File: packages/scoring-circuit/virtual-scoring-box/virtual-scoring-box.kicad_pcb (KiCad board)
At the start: 4 copper layers, 120 x 85 mm, 146 parts, among them J1 GCT USB4105-GF-A, J2 STM SWD 3.3V, J3 LEFT WEAPON A B C, J4 RIGHT WEAPON A B C, J5 PISTE - NOT protective earth, J6 ESP 3.3V UART recovery, J7 PRIMARY SWD PADS, SW1 STM RESET, SW2 ESP RESET, SW3 ESP BOOT, T1 750315371, U1 STM32G474RET6, U13 TSOP38438, U18 CP2102N-A02-GQFN20R, U19 ISO7021DR, U2 ESP32-S3-WROOM-1-N8R8, U20 TPS70933DBVR, U21 SN6505BDBVR, U22 TPS62162DSGR, U23 STUSB4500QTR, U24 STM32C011F6P6, U25 TPS259470ARPWR, U26 SN74LVC1G3208DBVR, U27 SN74LVC1T45DBVR, U3 TPD2E2U06DCKR, U8 74LVC125APW, U9 74LVC125APW, Y1 ABM3B-8.000MHZ-B2-T

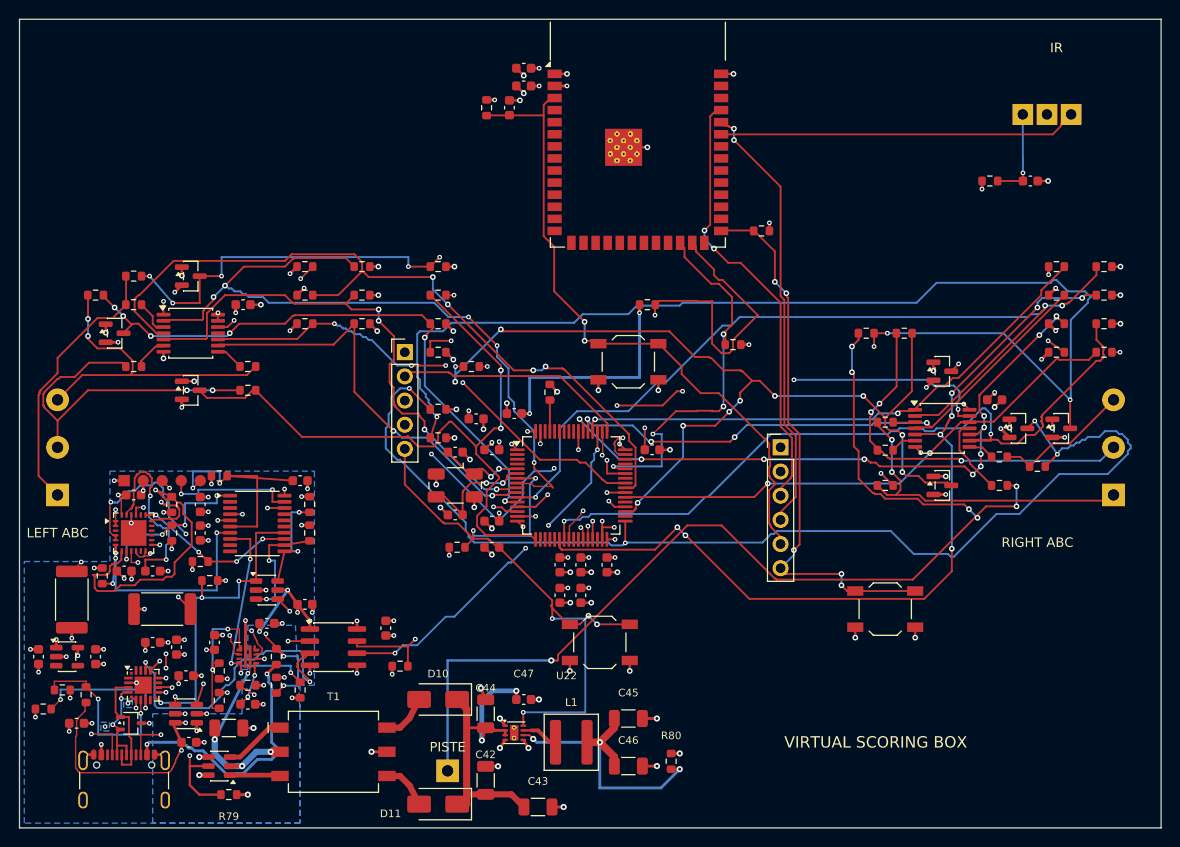
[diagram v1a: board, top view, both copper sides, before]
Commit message: fix(scoring-circuit): refine virtual-box layout and refresh assembly draft
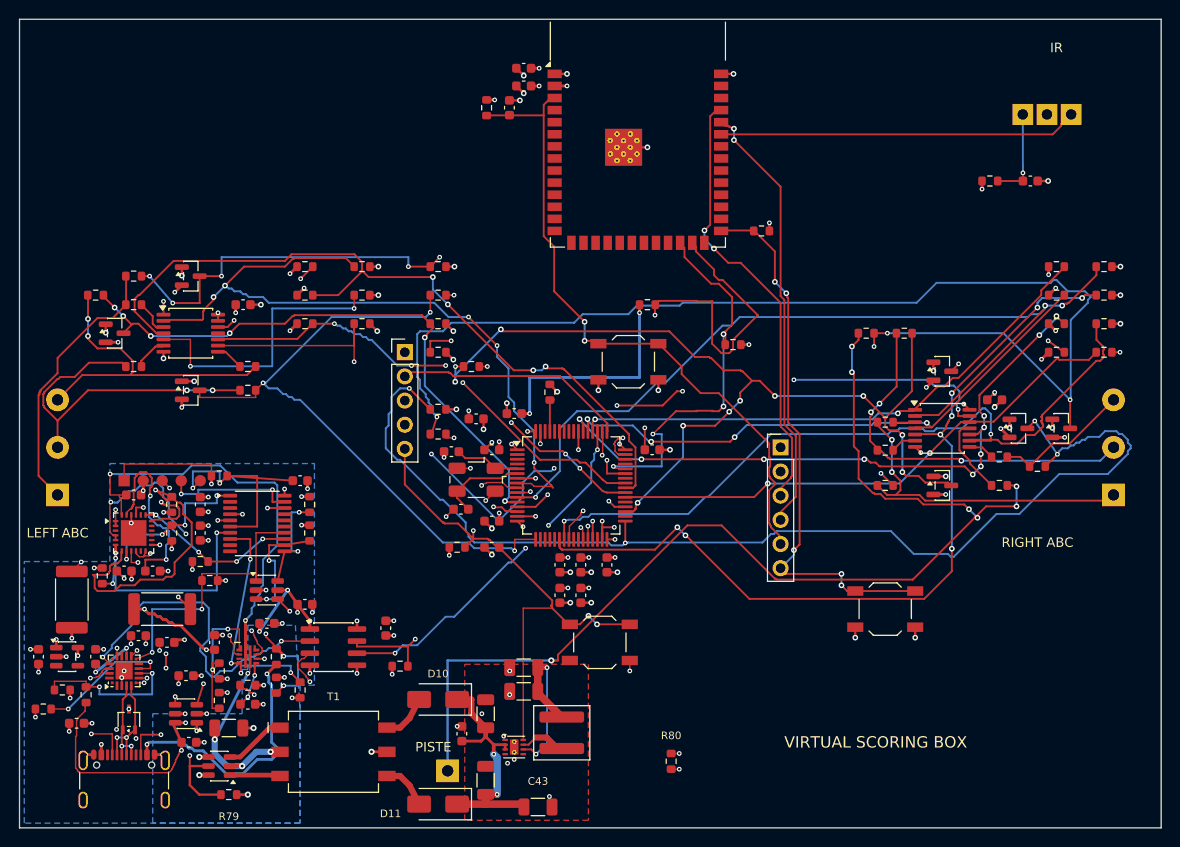
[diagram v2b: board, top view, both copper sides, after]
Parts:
- moved C46 15.1 mm to (103.0, 118.2), turned to 180 degrees
- moved C45 11.4 mm to (103.0, 120.7), turned to 180 degrees
- moved C47 7.43 mm to (96.5, 125.1), turned to 90 degrees
- moved C36 4.18 mm to (62.5, 114.8), turned to 0 degrees
- moved U18 2.50 mm to (61.0, 118.5), turned to 90 degrees
- moved Y1 2.28 mm to (98.0, 98.4)
- moved C35 1.50 mm to (65.5, 115.5)
- moved U22 1.50 mm to (102.0, 126.5)
- moved L1 1.41 mm to (107.0, 125.0), turned to 90 degrees
- moved C18 0.85 mm to (96.4, 101.5)
- moved U3 0.45 mm to (61.5, 123.6), turned to 90 degrees
- moved C17 0.40 mm to (95.4, 95.5), turned to 180 degrees
- moved R71 0.40 mm to (94.0, 93.6)
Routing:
- net USB_VBUS: track 74.3 -> 115.2 mm
- net LEFT_B_DRIVE: track 56.5 -> 77.6 mm, vias 4 -> 3
- net HOST_UART_RX: track 19.3 -> 35.8 mm
- net LEFT_A_OE_N: track 73.8 -> 89.8 mm, vias 3 -> 5
- net CORE_3V3: track 100.2 -> 88.5 mm
- net GND: track 87.0 -> 76.0 mm, vias 74 -> 72
- net HOST_UART_TX: track 32.9 -> 42.1 mm
- net USB_HOST_3V3: track 37.7 -> 46.0 mm
- net ISO_UNREG: track 34.1 -> 25.9 mm
- net USB_AWAKE: track 35.3 -> 29.9 mm, vias 3 -> 2
- net STM_RESET_N: track 74.2 -> 69.6 mm, vias 6 -> 4
- net LEFT_B_SENSE: track 72.6 -> 68.1 mm, vias 2 -> 3
- net LEFT_C_DRIVE: track 44.2 -> 48.2 mm
- net HSE_OUT: track 12.8 -> 9.48 mm, vias 2 -> 0
- net USB_HOST_DP: track 12.7 -> 9.40 mm, vias 0 -> 2
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- added copper zone on F.Cu, net GND
- added copper zone on In2.Cu, net USB_GND
- removed copper zone on B.Cu, net USB_GND

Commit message: refactor(scoring-circuit): organize virtual-box placement and routing
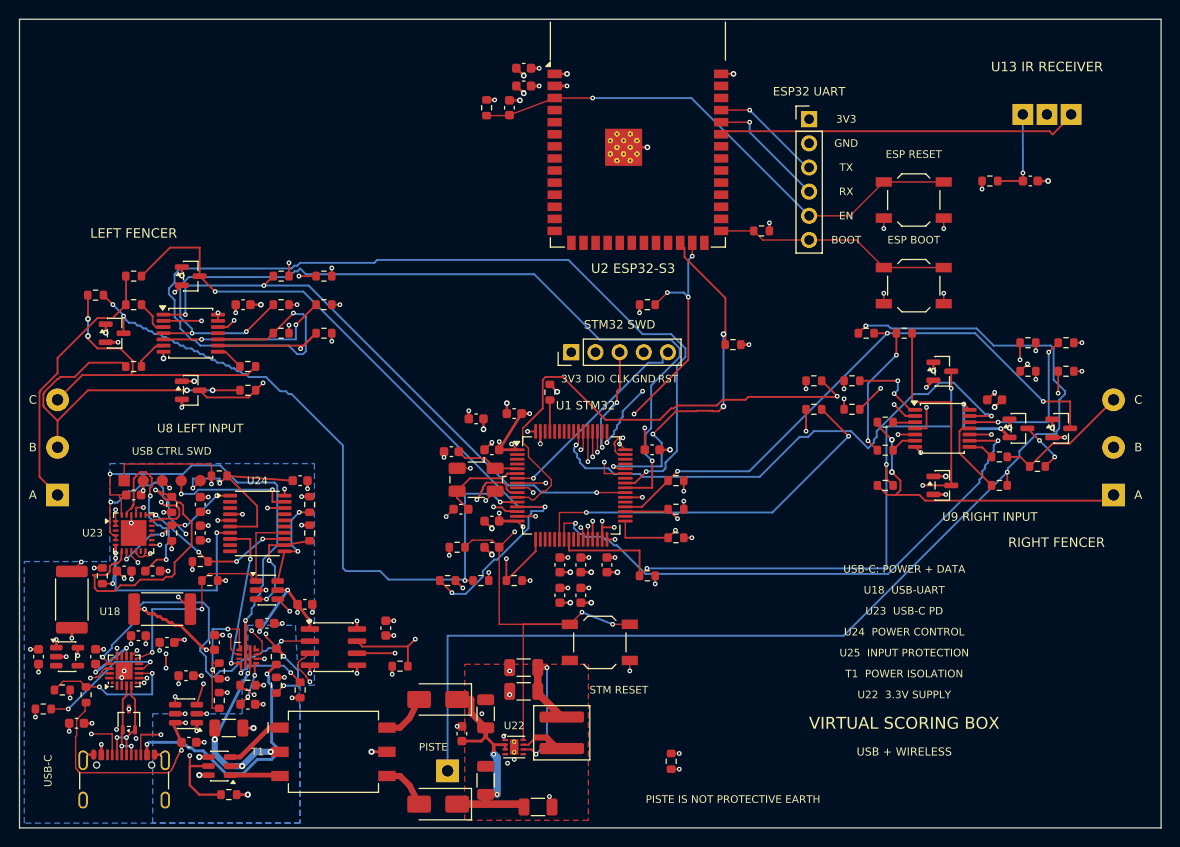
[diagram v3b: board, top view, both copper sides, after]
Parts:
- moved J6 34.6 mm to (133.0, 60.5)
- moved SW2 34.5 mm to (144.0, 69.0)
- moved SW3 34.1 mm to (144.0, 78.0)
- moved R65 33.0 mm to (95.0, 109.0)
- moved R48 32.8 mm to (133.5, 88.0), turned to 180 degrees
- moved R49 32.8 mm to (133.5, 91.0), turned to 180 degrees
- moved R68 32.2 mm to (116.0, 108.5)
- moved R66 31.0 mm to (102.0, 109.0)
- moved R70 28.4 mm to (119.0, 104.5)
- moved R67 27.4 mm to (98.5, 109.0)
- moved R69 26.2 mm to (119.0, 101.5)
- moved R71 25.5 mm to (119.0, 98.5)
- moved R18 24.6 mm to (137.5, 88.0)
- moved R21 24.6 mm to (137.5, 91.0)
- moved J2 17.5 mm to (108.0, 85.0), turned to 90 degrees
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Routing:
- net PISTE_SENSE: track 159.6 -> 61.5 mm, vias 5 -> 3
- net LEFT_C_OE_N: track 50.6 -> 111.5 mm, vias 4 -> 2
- net RIGHT_C_SENSE: track 120.1 -> 60.7 mm, vias 4 -> 3
- net RIGHT_A_SENSE: track 115.4 -> 67.5 mm, vias 4 -> 3
- net RIGHT_B_SENSE: track 99.1 -> 56.5 mm, vias 11 -> 2
- net RIGHT_B_DRIVE: track 89.5 -> 48.2 mm, vias 8 -> 3
- net ESP_PROGRAM_TX: track 46.7 -> 11.7 mm, vias 2 -> 1
- net ESP_PROGRAM_RX: track 46.1 -> 12.9 mm, vias 2 -> 1
- net ESP_BOOT0: track 57.8 -> 25.0 mm, vias 5 -> 0
- net RIGHT_A_DRIVE: track 93.1 -> 63.3 mm, vias 3 -> 2
- net LEFT_A_OE_N: track 89.8 -> 62.0 mm, vias 5 -> 3
- net LEFT_B_DRIVE: track 77.6 -> 55.5 mm
- net SWCLK: track 33.8 -> 12.6 mm, vias 3 -> 2
- net ESP_EN: track 70.2 -> 55.0 mm, vias 2 -> 1
- net STM_TX: track 49.5 -> 35.1 mm, vias 2 -> 5
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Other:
- board text added: "3V3"
- board text added: "A"
- board text added: "B"
- board text added: "BOOT"
- board text added: "C"
- board text added: "CLK"
- board text added: "DIO"
- board text added: "EN"
- board text added: "ESP BOOT"
- board text added: "ESP RESET"
- board text added: "ESP32 UART"
- board text added: "GND"
- board text added: "LEFT FENCER"
- board text added: "PISTE IS NOT PROTECTIVE EARTH"
- board text added: "RIGHT FENCER"
- board text added: "RST"
- board text added: "RX"
- board text added: "STM RESET"
- board text added: "STM32 SWD"
- board text added: "T1"
- board text added: "T1 POWER ISOLATION"
- board text added: "TX"
- board text added: "U1 STM32"
- board text added: "U13 IR RECEIVER"
- board text added: "U18"
- board text added: "U18 USB-UART"
- board text added: "U2 ESP32-S3"
- board text added: "U22"
- board text added: "U22 3.3V SUPPLY"
- board text added: "U23"
- board text added: "U23 USB-C PD"
- board text added: "U24"
- board text added: "U24 POWER CONTROL"
- board text added: "U25"
- board text added: "U25 INPUT PROTECTION"
- board text added: "U8 LEFT INPUT"
- board text added: "U9 RIGHT INPUT"
- board text added: "USB + WIRELESS"
- board text added: "USB CTRL SWD"
- board text added: "USB-C"
- board text added: "USB-C: POWER + DATA"
- board text removed: "IR"
- board text removed: "LEFT ABC"
- board text removed: "PARTIAL ROUTING - NOT FOR FABRICATION"
- board text removed: "POWER INTEGRATION PENDING"
- board text removed: "RIGHT ABC"

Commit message: style(scoring-circuit): simplify board labels and add Fencing Club brand
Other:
- board text added: "ESP32-S3"
- board text added: "FENCING CLUB"
- board text added: "IR RECEIVER"
- board text added: "LEFT INPUT"
- board text added: "RIGHT INPUT"
- board text added: "STM32"
- board text removed: "PISTE IS NOT PROTECTIVE EARTH"
- board text removed: "T1"
- board text removed: "T1 POWER ISOLATION"
- board text removed: "U1 STM32"
- board text removed: "U13 IR RECEIVER"
- board text removed: "U18"
- board text removed: "U18 USB-UART"
- board text removed: "U2 ESP32-S3"
- board text removed: "U22"
- board text removed: "U22 3.3V SUPPLY"
- board text removed: "U23"
- board text removed: "U23 USB-C PD"
- board text removed: "U24"
- board text removed: "U24 POWER CONTROL"
- board text removed: "U25"
- board text removed: "U25 INPUT PROTECTION"
- board text removed: "U8 LEFT INPUT"
- board text removed: "U9 RIGHT INPUT"
- board text removed: "USB-C: POWER + DATA"
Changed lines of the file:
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@@
 		(layer "User.2")
-	)
-	(gr_text "U23"
-		(at 57.675 104 0)
-		(layer "F.SilkS")
-		(effects
-			(font
-				(size 0.8 0.8)
-				(thickness 0.14)
-			)
-		)
-	)
-	(gr_text "U18"
-		(at 59.5 112.255 0)
-		(layer "F.SilkS")
-		(effects
-			(font
-				(size 0.8 0.8)
-				(thickness 0.14)
-			)
-		)
 	)
 	(gr_text "USB CTRL SWD"
@@
 		)
 	)
-	(gr_text "U24"
-		(at 75 98.505 0)
-		(layer "F.SilkS")
-		(effects
-			(font
-				(size 0.8 0.8)
-				(thickness 0.14)
-			)
-		)
-	)
-	(gr_text "T1"
-		(at 75.02 127 0)
-		(layer "F.SilkS")
-		(effects
-			(font
-				(size 0.8 0.8)
-				(thickness 0.14)
-			)
-		)
-	)
 	(gr_text "PISTE"
 		(at 93.5 126.5 0)
@@
 		)
 	)
-	(gr_text "U22"
-		(at 102 124.255 0)
-		(layer "F.SilkS")
-		(effects
-			(font
-				(size 0.8 0.8)
-				(thickness 0.14)
-			)
-		)
-	)
 	(gr_text "3V3"
 		(at 108 87.8 0)
@@
 		)
 	)
-	(gr_text "PISTE IS NOT PROTECTIVE EARTH"
-		(at 125 132 0)
-		(layer "F.SilkS")
-		(effects
-			(font
-				(size 0.8 0.8)
-				(thickness 0.14)
+	(gr_text "FENCING CLUB"
+		(at 143 118 0)
+		(layer "F.SilkS")
+		(effects
+			(font
+				(size 1.8 1.8)
+				(thickness 0.25)
 			)
 		)
@@
 		)
 	)
-	(gr_text "USB-C: POWER + DATA"
-		(at 143 107.8 0)
-		(layer "F.SilkS")
-		(effects
-			(font
-				(size 0.8 0.8)
-				(thickness 0.14)
-			)
-		)
-	)
-	(gr_text "U18  USB-UART"
-		(at 143 110 0)
-		(layer "F.SilkS")
-		(effects
-			(font
-				(size 0.8 0.8)
-				(thickness 0.14)
-			)
-		)
-	)
-	(gr_text "U23  USB-C PD"
-		(at 143 112.2 0)
-		(layer "F.SilkS")
-		(effects
-			(font
-				(size 0.8 0.8)
-				(thickness 0.14)
-			)
-		)
-	)
-	(gr_text "U24  POWER CONTROL"
-		(at 143 114.4 0)
-		(layer "F.SilkS")
-		(effects
-			(font
-				(size 0.8 0.8)
-				(thickness 0.14)
-			)
-		)
-	)
-	(gr_text "U25  INPUT PROTECTION"
-		(at 143 116.6 0)
-		(layer "F.SilkS")
-		(effects
-			(font
-				(size 0.8 0.8)
-				(thickness 0.14)
-			)
-		)
-	)
-	(gr_text "T1  POWER ISOLATION"
-		(at 143 118.8 0)
-		(layer "F.SilkS")
-		(effects
-			(font
-				(size 0.8 0.8)
-				(thickness 0.14)
-			)
-		)
-	)
-	(gr_text "U22  3.3V SUPPLY"
-		(at 143 121 0)
-		(layer "F.SilkS")
-		(effects
-			(font
-				(size 0.8 0.8)
-				(thickness 0.14)
-			)
-		)
-	)
 	(gr_text "ESP RESET"
 		(at 144 64.2 0)
@@
 		)
 	)
-	(gr_text "U8 LEFT INPUT"
+	(gr_text "LEFT INPUT"
 		(at 69 93 0)
 		(layer "F.SilkS")
@@
 		)
 	)
-	(gr_text "U1 STM32"
+	(gr_text "STM32"
 		(at 109.5 90.6 0)
 		(layer "F.SilkS")
@@
 		)
 	)
-	(gr_text "U9 RIGHT INPUT"
+	(gr_text "RIGHT INPUT"
 		(at 152 102.3 0)
 		(layer "F.SilkS")
@@
 		)
 	)
-	(gr_text "U2 ESP32-S3"
+	(gr_text "ESP32-S3"
 		(at 114.5 76.2 0)
 		(layer "F.SilkS")
@@
 		)
 	)
-	(gr_text "U13 IR RECEIVER"
+	(gr_text "IR RECEIVER"
 		(at 158 55 0)
 		(layer "F.SilkS")
@@
 		)
 	)
-	(gr_text "U25"
-		(at 74 117 0)
-		(layer "B.SilkS")
-		(effects
-			(font
-				(size 0.8 0.8)
-				(thickness 0.14)
-			)
-			(justify mirror)
-		)
-	)

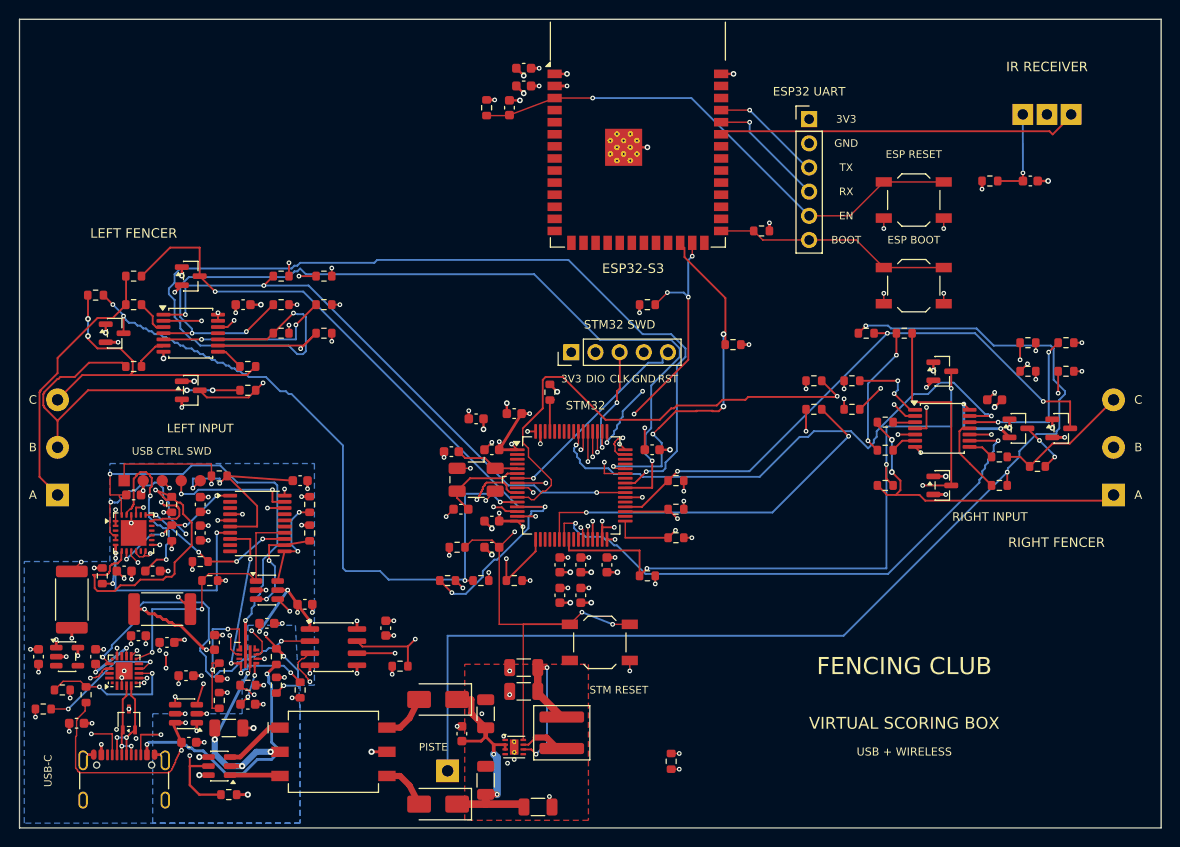
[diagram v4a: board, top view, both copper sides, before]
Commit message: refactor(scoring-circuit): move suitable virtual board routes to surface
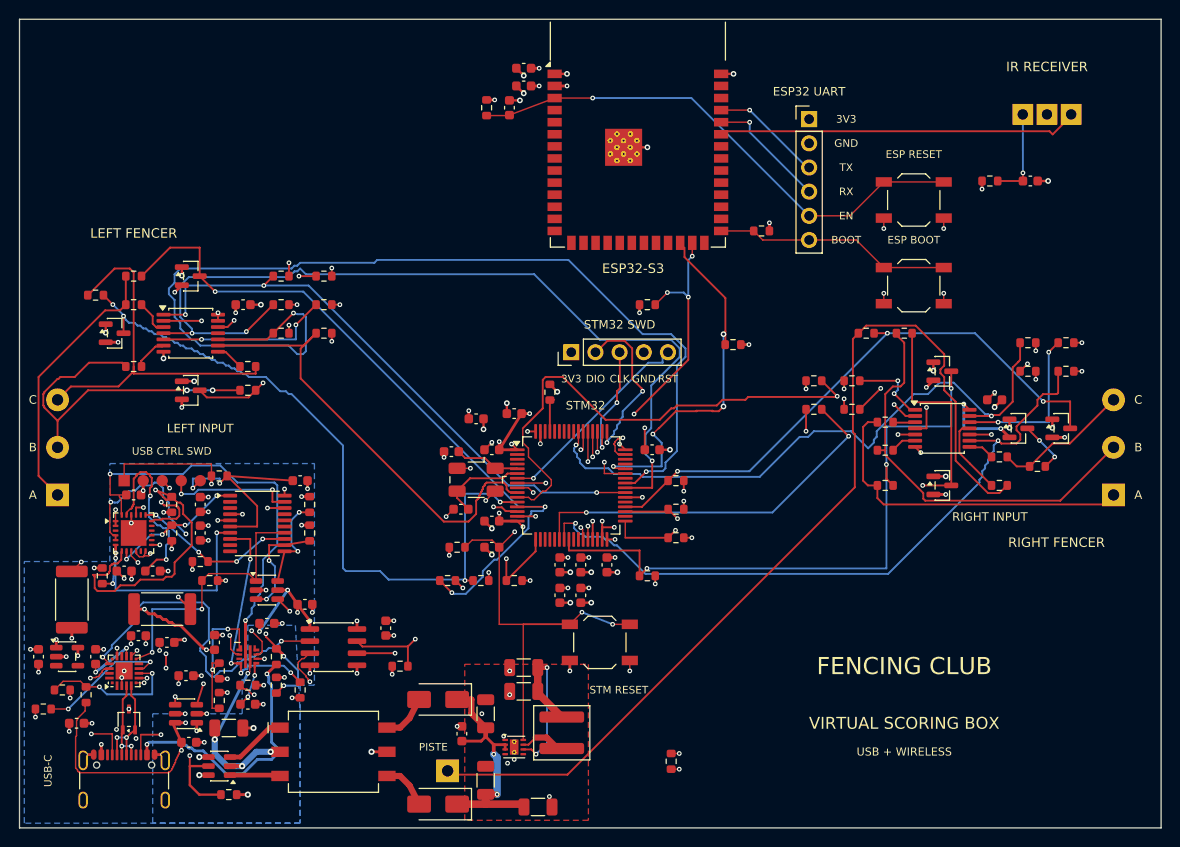
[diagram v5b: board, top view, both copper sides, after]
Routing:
- net PISTE: track 120.6 -> 101.8 mm, vias 2 -> 0
- net LEFT_C_DRIVE: track 56.1 -> 48.9 mm, vias 2 -> 0
- net LEFT_C: track 34.2 -> 40.1 mm, vias 2 -> 0
- net SWDIO: track 14.8 -> 17.7 mm
- net RIGHT_B: track 41.6 -> 43.9 mm, vias 2 -> 0
- net RIGHT_A: track 34.6 -> 36.3 mm, vias 2 -> 0
- net PISTE_OE_N: track 68.3 -> 66.9 mm, vias 3 -> 2
- net GND: track 76.6 -> 77.7 mm, vias 72 -> 73
- net RIGHT_C_DRIVE: track 73.9 -> 72.9 mm, vias 3 -> 2
